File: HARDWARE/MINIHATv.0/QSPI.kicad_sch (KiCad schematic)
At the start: 9 parts, among them U3 W25Q128JVS

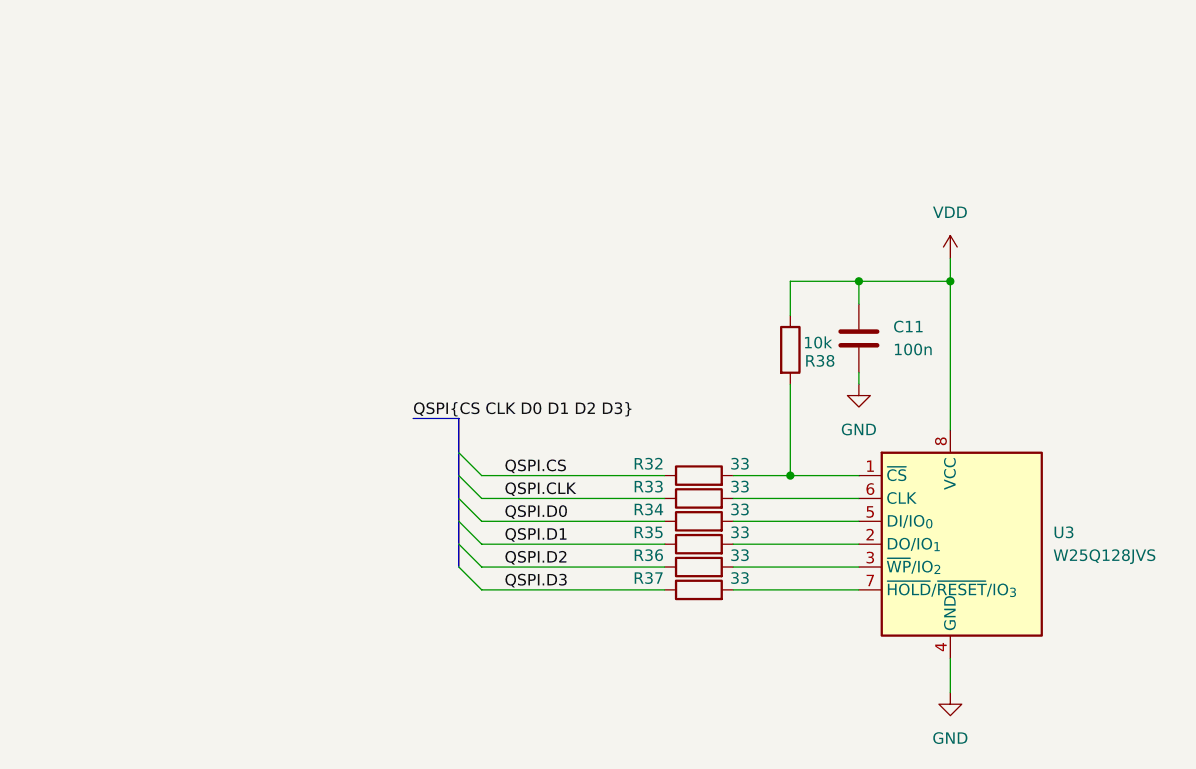
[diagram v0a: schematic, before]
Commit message: added normal buses
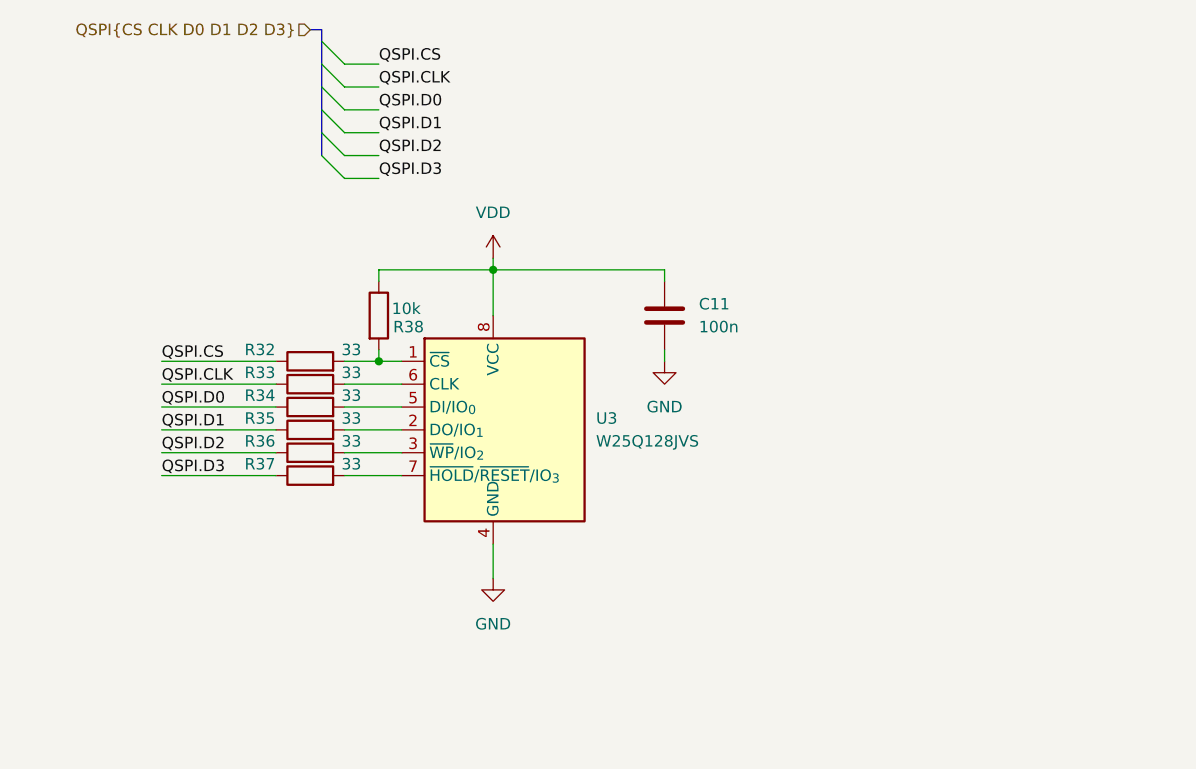
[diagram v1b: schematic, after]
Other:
- moved on the sheet: C11, R32, R33, R34, R35, R36, R37, R38, U3
